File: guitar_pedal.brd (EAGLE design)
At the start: 76.2 x 76.2 mm, 98 parts, among them P1 RM-065, P2 RM-065, P3 RM-065, U1 LM324NSOIC-14, U2 LM324NSOIC-14, U3 LM386N-3, U4 LM386N-3, U5 LM386N-3

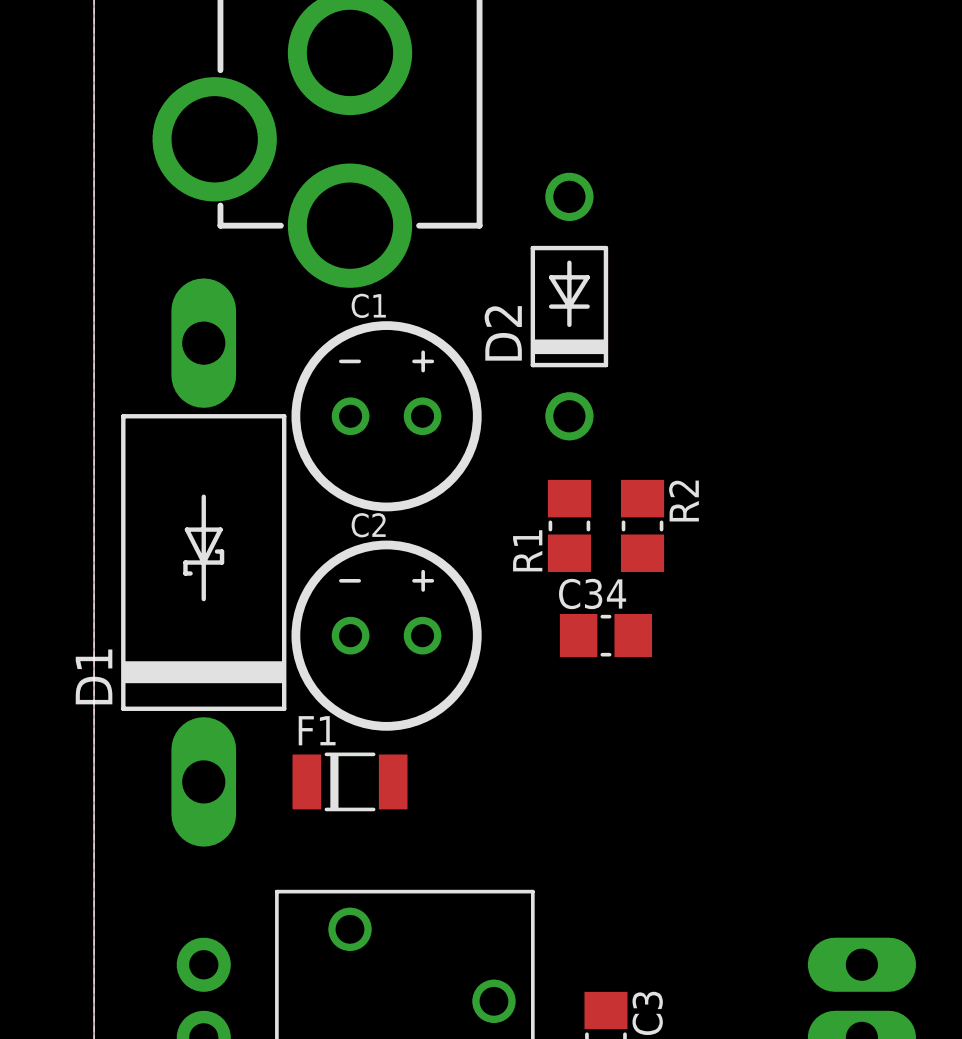
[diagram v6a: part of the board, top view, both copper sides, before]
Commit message: changed PTC to tayda 1.1A through hole component.
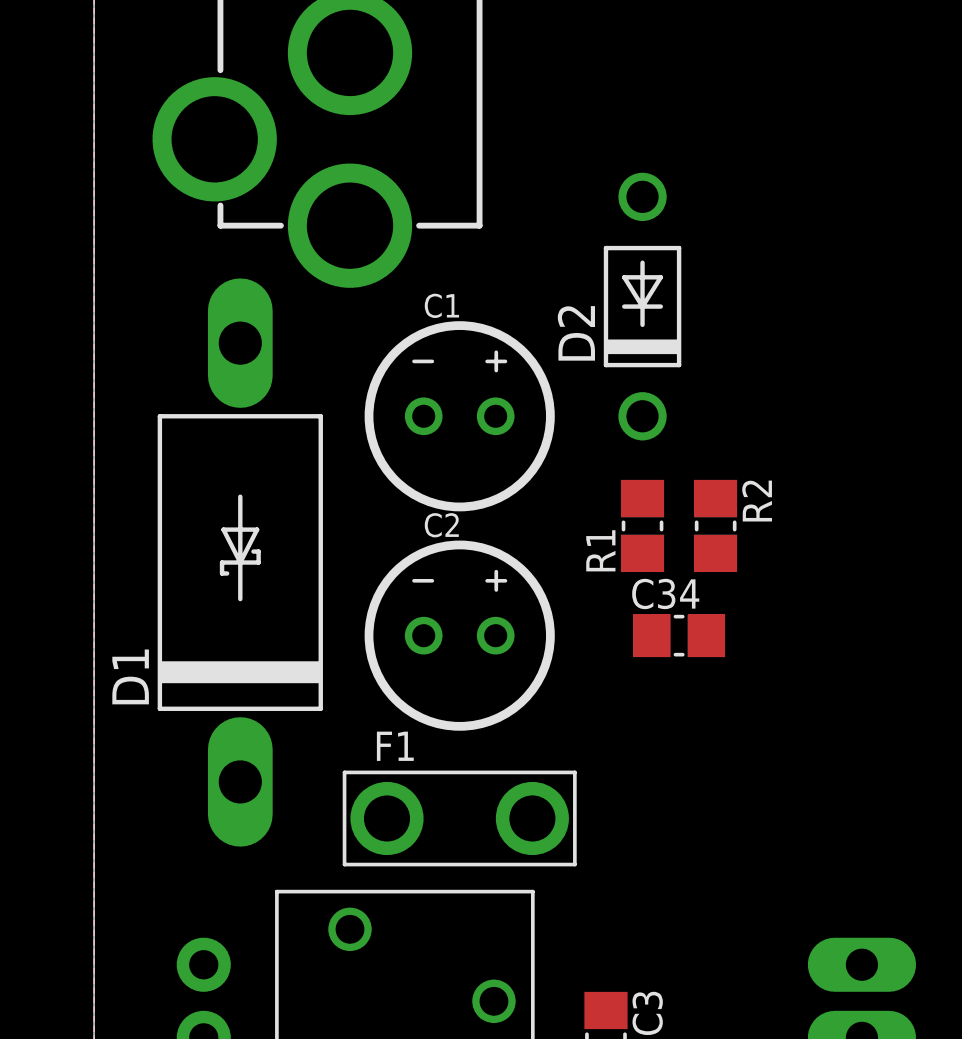
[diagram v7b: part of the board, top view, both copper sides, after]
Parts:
- F1: value PTCBELFUSE_1206 -> RUEF110 1.1A; device Luke:1206_PTC -> Luke:RADIAL_PTC_RUEF110
- moved F1 4.02 mm to (12.7, 45.7)
- moved C1 2.54 mm to (12.7, 59.7)
- moved C2 2.54 mm to (12.7, 52.1)
- moved C34 2.54 mm to (20.3, 52.1)
- moved D2 2.54 mm to (19.1, 63.5)
- moved R1 2.54 mm to (19.1, 55.9)
- moved R2 2.54 mm to (21.6, 55.9)
- moved D1 1.27 mm to (5.08, 54.6)
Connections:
- net +9V: now also F1.P$2; no longer F1.C
- net N$32: now also F1.P$1; no longer F1.A
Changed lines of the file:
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@@
 <attribute name="PROD_ID" value="CONN-08197" x="-11.43" y="81.28" size="1.778" layer="27" rot="R180" display="off"/>
 </element>
-<element name="D1" library="aarons" package="DO201T15" value="1N5822" x="3.81" y="54.61" rot="R90"/>
-<element name="D2" library="aarons" package="DO41-7" value="1n4739" x="16.51" y="63.5" rot="R90"/>
-<element name="R1" library="Luke" package="C0805" value="100k" x="16.51" y="55.88" rot="R90"/>
-<element name="R2" library="Luke" package="C0805" value="100k" x="19.05" y="55.88" rot="R270"/>
+<element name="D1" library="aarons" package="DO201T15" value="1N5822" x="5.08" y="54.61" rot="R90"/>
+<element name="D2" library="aarons" package="DO41-7" value="1n4739" x="19.05" y="63.5" rot="R90"/>
+<element name="R1" library="Luke" package="C0805" value="100k" x="19.05" y="55.88" rot="R90"/>
+<element name="R2" library="Luke" package="C0805" value="100k" x="21.59" y="55.88" rot="R270"/>
 <element name="P1" library="aarons" package="RM-065" value="RM-065" x="8.89" y="39.37" rot="R270"/>
 <element name="C3" library="Luke" package="C0805" value="1u" x="17.78" y="38.1" rot="R270"/>
@@
 <element name="U1" library="aarons" package="SOIC-14" value="LM324NSOIC-14" x="35.56" y="27.94" rot="R270"/>
 <element name="U2" library="aarons" package="SOIC-14" value="LM324NSOIC-14" x="41.91" y="69.85" rot="R90"/>
-<element name="C1" library="Luke" package="CAN_6MM" value="100uF 35v" x="10.16" y="59.69"/>
-<element name="C2" library="Luke" package="CAN_6MM" value="100uF 35v" x="10.16" y="52.07"/>
+<element name="C1" library="Luke" package="CAN_6MM" value="100uF 35v" x="12.7" y="59.69"/>
+<element name="C2" library="Luke" package="CAN_6MM" value="100uF 35v" x="12.7" y="52.07"/>
 <element name="R33" library="aarons" package="1X03_LONGPADS" value="100k" x="26.67" y="35.56" rot="MR90"/>
 <element name="R34" library="aarons" package="1X03_LONGPADS" value="100k" x="26.67" y="29.21" rot="MR270"/>
@@
 <element name="R42" library="aarons" package="1X03_LONGPADS" value="500k" x="50.8" y="58.42" rot="MR180"/>
 <element name="C21" library="Luke" package="CAN01" value="470uF" x="40.64" y="41.91" rot="R180"/>
-<element name="F1" library="Luke" package="1206_PTC" value="PTCBELFUSE_1206" x="8.89" y="46.99"/>
+<element name="F1" library="Luke" package="RADIAL_PTC_RUEF110" value="RUEF110 1.1A" x="12.7" y="45.72"/>
 <element name="C27" library="Luke" package="C0805" value="1uF" x="64.77" y="49.53"/>
 <element name="C28" library="Luke" package="C0805" value="1uF" x="60.96" y="34.29"/>
@@
 <element name="C32" library="Luke" package="C0805" value="1uF" x="26.67" y="32.385" rot="R180"/>
 <element name="C33" library="Luke" package="C0805" value="1uF" x="12.065" y="25.4" rot="R180"/>
-<element name="C34" library="Luke" package="C0805" value="1uF" x="17.78" y="52.07"/>
+<element name="C34" library="Luke" package="C0805" value="1uF" x="20.32" y="52.07"/>
 </elements>
 <signals>
@@
 <contactref element="R2" pad="2"/>
 <contactref element="C34" pad="1"/>
-<wire x1="16.51" y1="54.93" x2="19.05" y2="54.93" width="0" layer="19" extent="1-1"/>
-<wire x1="16.83" y1="52.07" x2="16.51" y2="54.93" width="0" layer="19" extent="1-1"/>
-<wire x1="32.2453" y1="29.845" x2="16.83" y2="52.07" width="0" layer="19" extent="1-1"/>
+<wire x1="19.05" y1="54.93" x2="21.59" y2="54.93" width="0" layer="19" extent="1-1"/>
+<wire x1="19.37" y1="52.07" x2="19.05" y2="54.93" width="0" layer="19" extent="1-1"/>
+<wire x1="32.2453" y1="29.845" x2="19.37" y2="52.07" width="0" layer="19" extent="1-1"/>
 <wire x1="32.2453" y1="27.305" x2="32.2453" y2="29.845" width="0" layer="19" extent="1-1"/>
 <wire x1="38.8747" y1="29.845" x2="32.2453" y2="29.845" width="0" layer="19" extent="1-1"/>
@@
 <contactref element="U5" pad="6"/>
 <contactref element="C26" pad="+"/>
-<contactref element="F1" pad="C"/>
+<contactref element="F1" pad="P$2"/>
 <contactref element="C28" pad="1"/>
 <contactref element="C27" pad="1"/>
@@
 <wire x1="13.015" y1="25.4" x2="27.62" y2="32.385" width="0" layer="19" extent="1-1"/>
 <wire x1="13.015" y1="22.86" x2="13.015" y2="25.4" width="0" layer="19" extent="1-1"/>
-<wire x1="10.39" y1="46.99" x2="13.015" y2="25.4" width="0" layer="19" extent="1-1"/>
-<wire x1="11.41" y1="52.07" x2="10.39" y2="46.99" width="0" layer="19" extent="1-1"/>
-<wire x1="16.51" y1="56.83" x2="11.41" y2="52.07" width="0" layer="19" extent="1-1"/>
-<wire x1="16.51" y1="59.69" x2="16.51" y2="56.83" width="0" layer="19" extent="1-1"/>
-<wire x1="11.41" y1="59.69" x2="16.51" y2="59.69" width="0" layer="19" extent="1-1"/>
+<wire x1="15.225" y1="45.72" x2="27.62" y2="32.385" width="0" layer="19" extent="1-1"/>
+<wire x1="13.95" y1="52.07" x2="15.225" y2="45.72" width="0" layer="19" extent="1-1"/>
+<wire x1="19.05" y1="56.83" x2="13.95" y2="52.07" width="0" layer="19" extent="1-1"/>
+<wire x1="19.05" y1="59.69" x2="19.05" y2="56.83" width="0" layer="19" extent="1-1"/>
+<wire x1="13.95" y1="59.69" x2="19.05" y2="59.69" width="0" layer="19" extent="1-1"/>
 </signal>
 <signal name="AMP_1">
@@
 <contactref element="JP7" pad="PWR"/>
 <contactref element="D1" pad="A"/>
-<wire x1="3.81" y1="62.23" x2="8.89" y2="66.31" width="0" layer="19" extent="1-1"/>
+<wire x1="5.08" y1="62.23" x2="8.89" y2="66.31" width="0" layer="19" extent="1-1"/>
 </signal>
 <signal name="GTR_IN">
@@
 <signal name="N$32">
 <contactref element="D1" pad="C"/>
-<contactref element="F1" pad="A"/>
-<wire x1="3.81" y1="46.99" x2="7.39" y2="46.99" width="0" layer="19" extent="1-1"/>
+<contactref element="F1" pad="P$1"/>
+<wire x1="5.08" y1="46.99" x2="10.175" y2="45.72" width="0" layer="19" extent="1-1"/>
 </signal>
 <signal name="N$2">

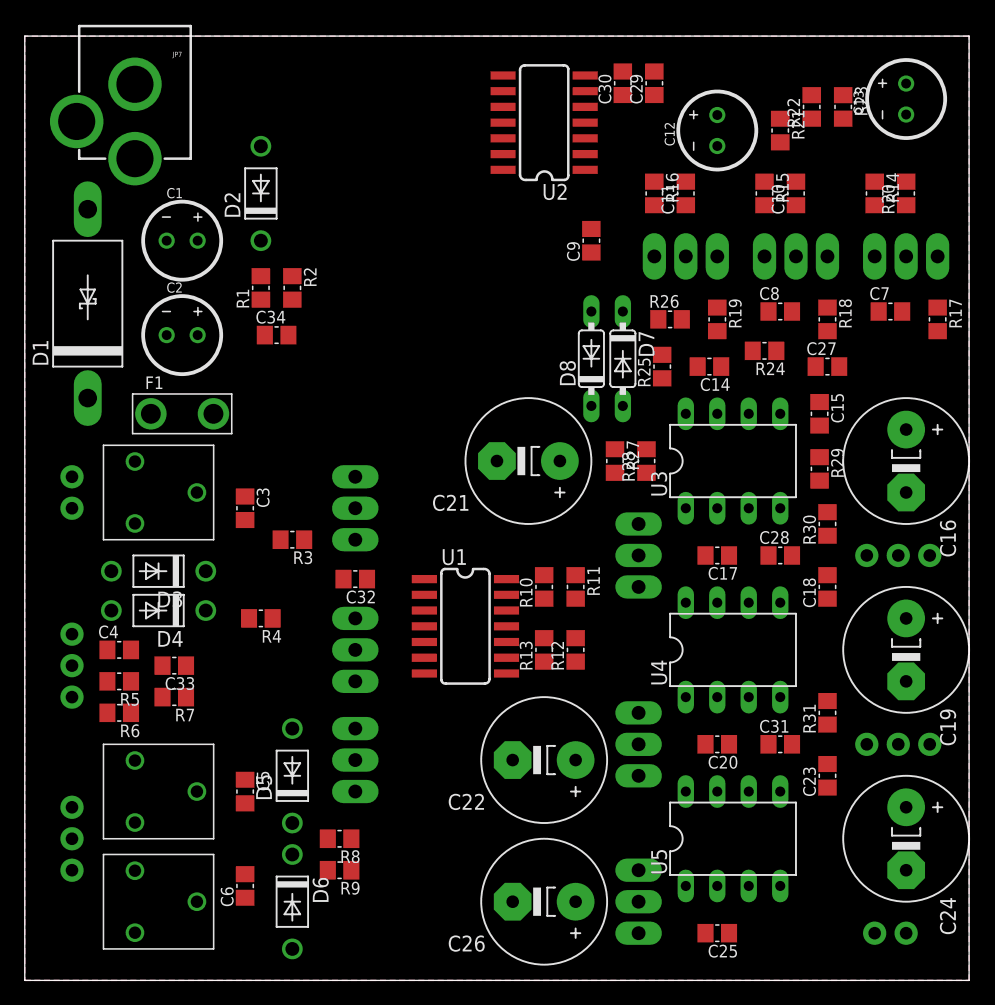
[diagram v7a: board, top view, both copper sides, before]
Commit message: Finished layout! Still need silk screen.
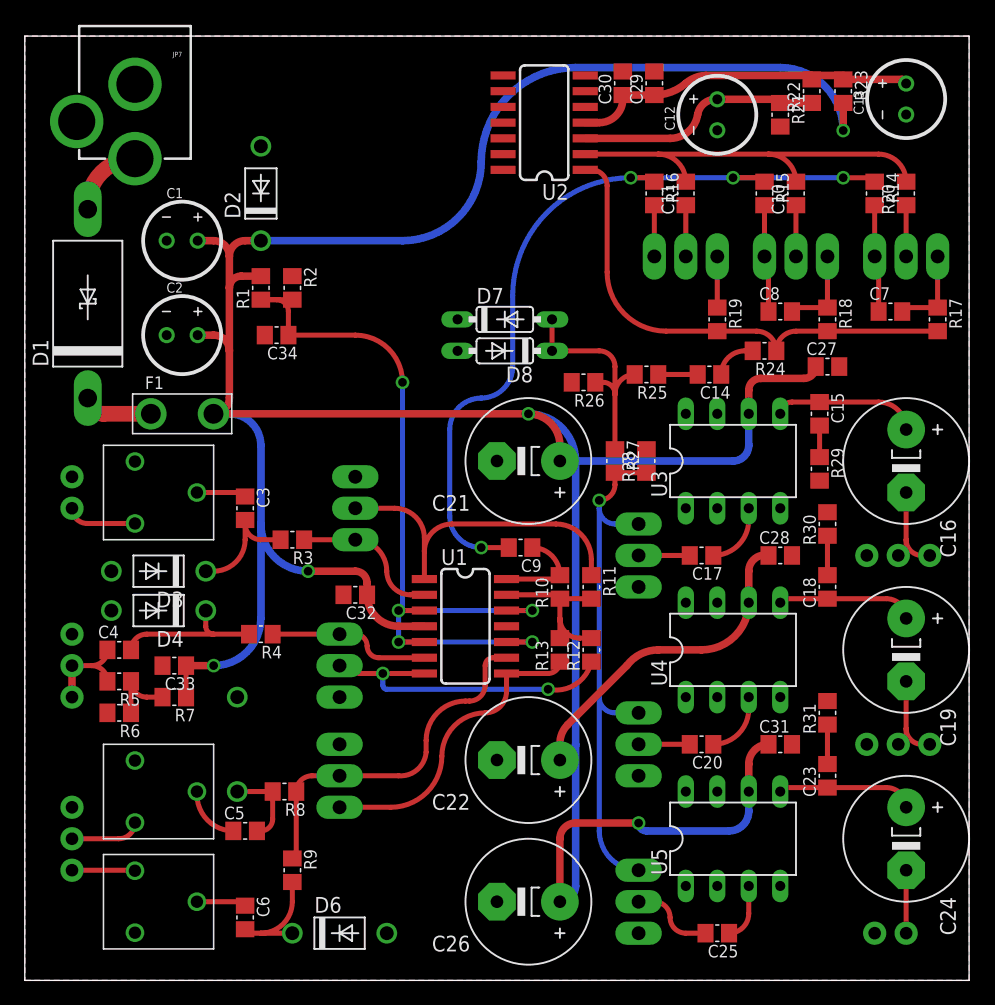
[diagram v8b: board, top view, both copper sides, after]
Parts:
- moved C9 25.4 mm to (40.0, 34.9), turned to 180 degrees
- moved D7 10.0 mm to (38.7, 53.3), turned to 0 degrees
- moved R26 8.64 mm to (45.1, 48.3), turned to 180 degrees
- moved D8 7.01 mm to (38.7, 50.8), turned to 180 degrees
- moved R8 5.85 mm to (21.0, 15.2)
- moved D5 5.12 mm to (17.1, 19.1), flipped to the bottom
- moved D6 4.58 mm to (25.4, 3.81), turned to 0 degrees
- moved R9 3.81 mm to (21.6, 8.89), turned to 270 degrees
- moved C5 3.18 mm to (17.8, 12.1), turned to 0 degrees
- moved C6 2.54 mm to (17.8, 5.08), turned to 270 degrees
- moved R34 1.80 mm to (25.4, 27.9)
- moved R35 1.80 mm to (25.4, 19.1)
- moved R25 1.42 mm to (50.2, 48.9), turned to 180 degrees
- moved C17 1.27 mm to (54.6, 34.3)
- moved C20 1.27 mm to (54.6, 19.1)
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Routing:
- net +9V: track 0.00 -> 281.2 mm, vias 0 -> 5
- net 4.5: track 0.00 -> 68.9 mm, vias 0 -> 5
- net N$12: track 0.00 -> 63.7 mm, vias 0 -> 4
- net PWR_AMP: track 0.00 -> 43.9 mm, vias 0 -> 1
- net FDBK: track 0.00 -> 39.2 mm
- net OUT_MIX: track 0.00 -> 33.1 mm
- net AMP_3: track 0.00 -> 28.4 mm
- net N$5: track 0.00 -> 28.2 mm
- net OUT_1: track 0.00 -> 26.7 mm
- net OUT_2: track 0.00 -> 25.8 mm, vias 0 -> 2
- net OUT_3: track 0.00 -> 23.5 mm
- net N$26: track 0.00 -> 19.7 mm
- net N$21: track 0.00 -> 19.1 mm
- net N$7: track 0.00 -> 13.4 mm
- net AMP_2: track 0.00 -> 13.0 mm
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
